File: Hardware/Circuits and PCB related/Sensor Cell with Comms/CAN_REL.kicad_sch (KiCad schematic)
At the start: 28 parts, among them U7 TCAN337, U8 MCP2518FD-xQBB, Y1 DSC6111B

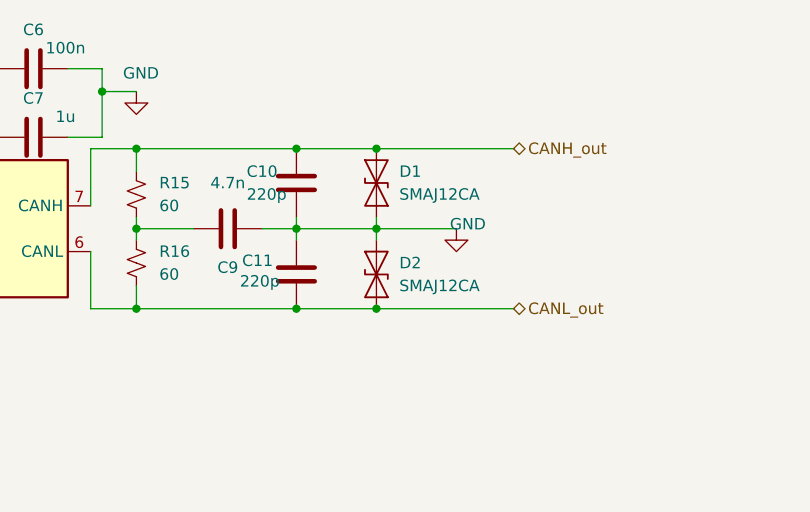
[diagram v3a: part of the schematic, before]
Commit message: Rev2 PCB finished, need to document and catalog for Iowa Innovation challenge this thursday
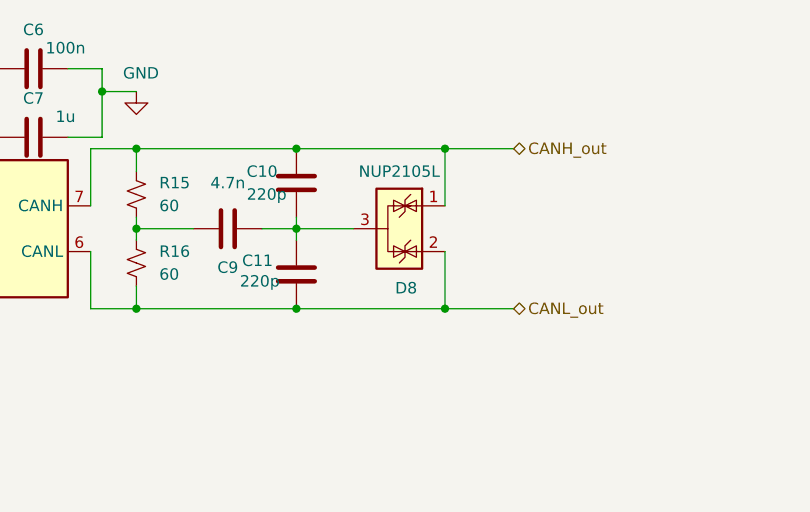
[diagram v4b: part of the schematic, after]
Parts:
- removed D1, D2: SMAJ12CA, Diode_SMD:D_SMA, symbol Diode:SMAJ12CA
- added D8: NUP2105L, Package_TO_SOT_SMD:SOT-23, symbol Power_Protection:NUP2105L
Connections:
- net CANH_out: now also D8.1 (K)
- net CANL_out: now also D8.2 (K)
- net GND: no longer C10.1, C11.2, C9.2
- new net: C10.1, C11.2, C9.2, D8.3 (A)
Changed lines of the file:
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@@
 	)
 	(junction
-		(at 110.49 50.8)
-		(diameter 0)
-		(color 0 0 0 0)
-	)
-	(junction
 		(at 101.6 33.02)
 		(diameter 0)
@@
 	)
 	(junction
-		(at 110.49 41.91)
+		(at 118.11 33.02)
 		(diameter 0)
 		(color 0 0 0 0)
@@
 	)
 	(junction
-		(at 110.49 33.02)
-		(diameter 0)
-		(color 0 0 0 0)
-	)
-	(junction
 		(at 101.6 41.91)
 		(diameter 0)
@@
 	)
 	(junction
+		(at 118.11 50.8)
+		(diameter 0)
+		(color 0 0 0 0)
+	)
+	(junction
 		(at 83.82 33.02)
 		(diameter 0)
@@
 	(wire
 		(pts
-			(xy 101.6 33.02) (xy 110.49 33.02)
+			(xy 101.6 33.02) (xy 118.11 33.02)
 		)
 		(stroke
@@
 	(wire
 		(pts
+			(xy 118.11 44.45) (xy 118.11 50.8)
+		)
+		(stroke
+			(width 0)
+			(type default)
+		)
+	)
+	(wire
+		(pts
 			(xy 78.74 39.37) (xy 78.74 33.02)
 		)
@@
 	(wire
 		(pts
-			(xy 153.67 127) (xy 158.75 127)
+			(xy 118.11 50.8) (xy 125.73 50.8)
 		)
 		(stroke
@@
 	(wire
 		(pts
-			(xy 134.62 83.82) (xy 134.62 86.36)
+			(xy 153.67 127) (xy 158.75 127)
 		)
 		(stroke
@@
 	(wire
 		(pts
-			(xy 93.98 151.13) (xy 93.98 152.4)
+			(xy 134.62 83.82) (xy 134.62 86.36)
 		)
 		(stroke
@@
 	(wire
 		(pts
-			(xy 110.49 40.64) (xy 110.49 41.91)
+			(xy 93.98 151.13) (xy 93.98 152.4)
 		)
 		(stroke
@@
 	(wire
 		(pts
+			(xy 101.6 41.91) (xy 107.95 41.91)
+		)
+		(stroke
+			(width 0)
+			(type default)
+		)
+	)
+	(wire
+		(pts
 			(xy 45.72 31.75) (xy 45.72 36.83)
 		)
@@
 	(wire
 		(pts
-			(xy 110.49 33.02) (xy 125.73 33.02)
-		)
-		(stroke
-			(width 0)
-			(type default)
-		)
-	)
-	(wire
-		(pts
 			(xy 119.38 107.95) (xy 104.14 107.95)
 		)
@@
 	(wire
 		(pts
-			(xy 101.6 50.8) (xy 110.49 50.8)
-		)
-		(stroke
-			(width 0)
-			(type default)
-		)
-	)
-	(wire
-		(pts
 			(xy 78.74 100.33) (xy 93.98 100.33)
 		)
@@
 	(wire
 		(pts
-			(xy 119.38 41.91) (xy 110.49 41.91)
-		)
-		(stroke
-			(width 0)
-			(type default)
-		)
-	)
-	(wire
-		(pts
 			(xy 102.87 97.79) (xy 97.79 97.79)
 		)
@@
 	(wire
 		(pts
-			(xy 110.49 41.91) (xy 110.49 43.18)
-		)
-		(stroke
-			(width 0)
-			(type default)
-		)
-	)
-	(wire
-		(pts
 			(xy 87.63 133.35) (xy 93.98 133.35)
 		)
@@
 	(wire
 		(pts
-			(xy 110.49 50.8) (xy 125.73 50.8)
+			(xy 101.6 50.8) (xy 118.11 50.8)
 		)
 		(stroke
@@
 	(wire
 		(pts
-			(xy 93.98 149.86) (xy 93.98 151.13)
+			(xy 118.11 33.02) (xy 125.73 33.02)
 		)
 		(stroke
@@
 	(wire
 		(pts
-			(xy 110.49 41.91) (xy 101.6 41.91)
+			(xy 93.98 149.86) (xy 93.98 151.13)
 		)
 		(stroke
@@
 	(wire
 		(pts
+			(xy 118.11 33.02) (xy 118.11 39.37)
+		)
+		(stroke
+			(width 0)
+			(type default)
+		)
+	)
+	(wire
+		(pts
 			(xy 109.22 95.25) (xy 119.38 95.25)
 		)
@@
 	)
 	(symbol
-		(lib_id "Diode:SMAJ12CA")
-		(at 110.49 36.83 90)
-		(unit 1)
-		(exclude_from_sim no)
-		(in_bom yes)
-		(on_board yes)
-		(dnp no)
-		(fields_autoplaced yes)
-		(property "Reference" "D1"
-			(at 113.03 35.5599 90)
-			(effects
-				(font
-					(size 1.27 1.27)
-				)
-				(justify right)
-			)
-		)
-		(property "Value" "SMAJ12CA"
-			(at 113.03 38.0999 90)
-			(effects
-				(font
-					(size 1.27 1.27)
-				)
-				(justify right)
-			)
-		)
-		(property "Footprint" "Diode_SMD:D_SMA"
-			(at 115.57 36.83 0)
-			(effects
-				(font
-					(size 1.27 1.27)
-				)
-				(hide yes)
-			)
-		)
-		(property "Datasheet" "https://www.littelfuse.com/media?resourcetype=datasheets&itemid=75e32973-b177-4ee3-a0ff-cedaf1abdb93&filename=smaj-datasheet"
-			(at 110.49 36.83 0)
-			(effects
-				(font
-					(size 1.27 1.27)
-				)
-				(hide yes)
-			)
-		)
-		(property "Description" "400W bidirectional Transient Voltage Suppressor, 12.0Vr, SMA(DO-214AC)"
-			(at 110.49 36.83 0)
-			(effects
-				(font
-					(size 1.27 1.27)
-				)
-				(hide yes)
-			)
-		)
-		(pin "2"
-		)
-		(pin "1"
-		)
-		(instances
-			(project "Sensor Cell with Comms"
-				(path "/953799b5-f11e-4770-941d-f5d23acc5c6d/779df1c1-ac91-4afc-a9dd-e99c8e3614d8"
-					(reference "D1")
-					(unit 1)
-				)
-			)
-		)
-	)
-	(symbol
 		(lib_id "Device:R_Small_US")
 		(at 53.34 49.53 180)
@@
 	)
 	(symbol
-		(lib_id "power:GND")
-		(at 119.38 41.91 0)
-		(unit 1)
-		(exclude_from_sim no)
-		(in_bom yes)
-		(on_board yes)
-		(dnp no)
-		(property "Reference" "#PWR048"
-			(at 119.38 48.26 0)
-			(effects
-				(font
-					(size 1.27 1.27)
-				)
-				(hide yes)
-			)
-		)
-		(property "Value" "GND"
-			(at 120.65 41.402 0)
-			(effects
-				(font
-					(size 1.27 1.27)
-				)
-			)
-		)
-		(property "Footprint" ""
-			(at 119.38 41.91 0)
-			(effects
-				(font
-					(size 1.27 1.27)
-				)
-				(hide yes)
-			)
-		)
-		(property "Datasheet" ""
-			(at 119.38 41.91 0)
-			(effects
-				(font
-					(size 1.27 1.27)
-				)
-				(hide yes)
-			)
-		)
-		(property "Description" "Power symbol creates a global label with name \"GND\" , ground"
-			(at 119.38 41.91 0)
-			(effects
-				(font
-					(size 1.27 1.27)
-				)
-				(hide yes)
-			)
-		)
-		(pin "1"
-		)
-		(instances
-			(project "Sensor Cell with Comms"
-				(path "/953799b5-f11e-4770-941d-f5d23acc5c6d/779df1c1-ac91-4afc-a9dd-e99c8e3614d8"
-					(reference "#PWR048")
-					(unit 1)
-				)
-			)
-		)
-	)
-	(symbol
-		(lib_id "Diode:SMAJ12CA")
-		(at 110.49 46.99 90)
-		(unit 1)
-		(exclude_from_sim no)
-		(in_bom yes)
-		(on_board yes)
-		(dnp no)
-		(fields_autoplaced yes)
-		(property "Reference" "D2"
-			(at 113.03 45.7199 90)
-			(effects
-				(font
-					(size 1.27 1.27)
-				)
-				(justify right)
-			)
-		)
-		(property "Value" "SMAJ12CA"
-			(at 113.03 48.2599 90)
-			(effects
-				(font
-					(size 1.27 1.27)
-				)
-				(justify right)
-			)
-		)
-		(property "Footprint" "Diode_SMD:D_SMA"
-			(at 115.57 46.99 0)
-			(effects
-				(font
-					(size 1.27 1.27)
-				)
-				(hide yes)
-			)
-		)
-		(property "Datasheet" "https://www.littelfuse.com/media?resourcetype=datasheets&itemid=75e32973-b177-4ee3-a0ff-cedaf1abdb93&filename=smaj-datasheet"
-			(at 110.49 46.99 0)
-			(effects
-				(font
-					(size 1.27 1.27)
-				)
-				(hide yes)
-			)
-		)
-		(property "Description" "400W bidirectional Transient Voltage Suppressor, 12.0Vr, SMA(DO-214AC)"
-			(at 110.49 46.99 0)
-			(effects
-				(font
-					(size 1.27 1.27)
-				)
-				(hide yes)
-			)
-		)
-		(pin "2"
-		)
-		(pin "1"
-		)
-		(instances
-			(project "Sensor Cell with Comms"
-				(path "/953799b5-f11e-4770-941d-f5d23acc5c6d/779df1c1-ac91-4afc-a9dd-e99c8e3614d8"
-					(reference "D2")
-					(unit 1)
-				)
-			)
-		)
-	)
-	(symbol
 		(lib_id "power:+3V3")
 		(at 43.18 52.07 0)
@@
 					(unit 1)
 				)
+			)
+		)
+	)
+	(symbol
+		(lib_id "Power_Protection:NUP2105L")
+		(at 113.03 41.91 270)
+		(unit 1)
+		(exclude_from_sim no)
+		(in_bom yes)
+		(on_board yes)
+		(dnp no)
+		(property "Reference" "D8"
+			(at 113.792 48.514 90)
+			(effects
+				(font
+					(size 1.27 1.27)
+				)
+			)
+		)
+		(property "Value" "NUP2105L"
+			(at 113.03 35.56 90)
+			(effects
+				(font
+					(size 1.27 1.27)
+				)
+			)
+		)
+		(property "Footprint" "Package_TO_SOT_SMD:SOT-23"
+			(at 111.76 47.625 0)
+			(effects
+				(font
+					(size 1.27 1.27)
+				)
+				(justify left)
+				(hide yes)
+			)
+		)
+		(property "Datasheet" "https://www.onsemi.com/pub_link/Collateral/NUP2105L-D.PDF"
+			(at 116.205 45.085 0)
+			(effects
+				(font
+					(size 1.27 1.27)
+				)
+				(hide yes)
+			)
+		)
+		(property "Description" "Dual Line CAN Bus Protector, 24Vrwm"
+			(at 113.03 41.91 0)
+			(effects
+				(font
+					(size 1.27 1.27)
+				)
+				(hide yes)
+			)
+		)
+		(pin "3"
+		)
+		(pin "1"
+		)
+		(pin "2"
+		)
+		(instances
+			(project ""
+				(path "/953799b5-f11e-4770-941d-f5d23acc5c6d/779df1c1-ac91-4afc-a9dd-e99c8e3614d8"
+					(reference "D8")
+					(unit 1)
+				)
